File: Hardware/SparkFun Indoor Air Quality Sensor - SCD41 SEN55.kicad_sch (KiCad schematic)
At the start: 38 parts, among them J1 Qwiic_RA, J2 Qwiic_RA, J3 Conn_01x04, U1 AP3012, U1 SEN55, U3 SCD41, U4 SEN55_Outline

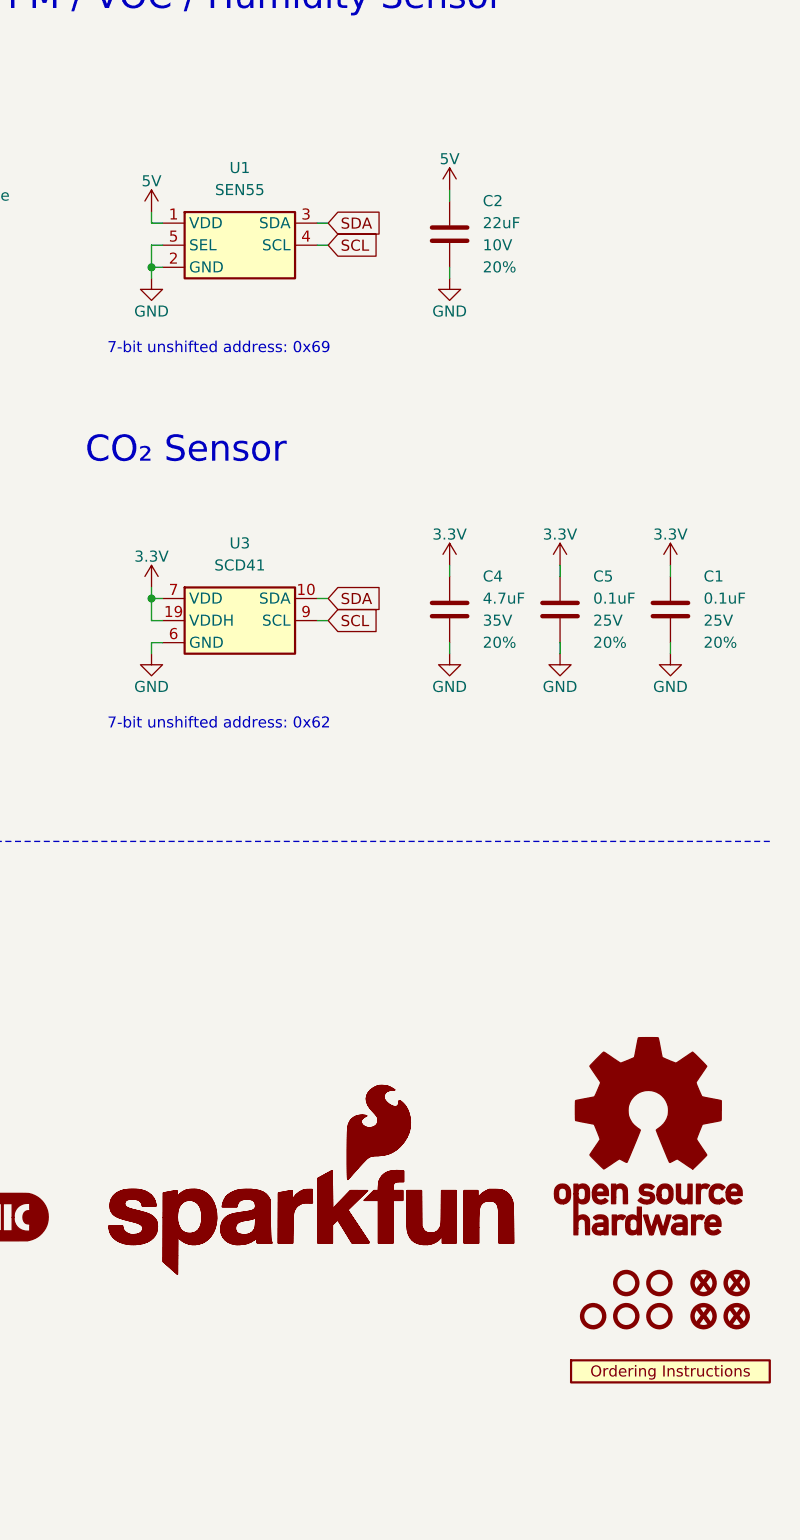
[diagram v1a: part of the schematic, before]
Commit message: Fix PROD_ID on SEN55 connector and module.
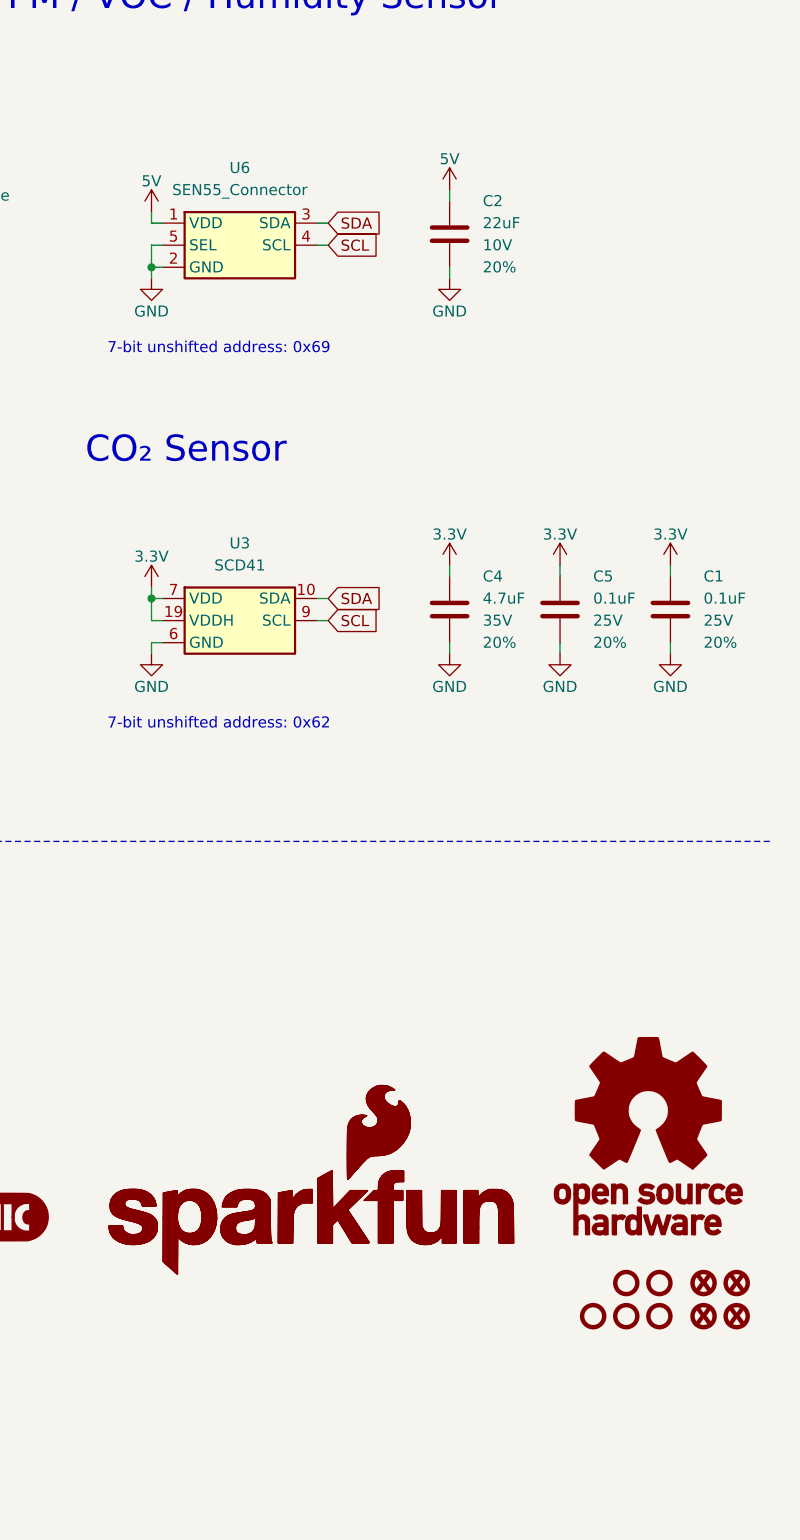
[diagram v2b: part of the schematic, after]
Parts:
- removed U1: SEN55, SparkFun-Connector:JST_SMD_1.25mm-6_Locking, symbol SparkFun-Sensor:SEN55
- removed U2: ~, SparkFun-Aesthetic:Ordering_Instructions, symbol SparkFun-Aesthetic:Ordering_Instructions
- added U6: SEN55_Connector, SparkFun-Connector:JST_SMD_1.25mm-6_Locking, symbol SparkFun-Sensor:SEN55_Connector
- U4: PROD_ID (none) -> COMP-20319
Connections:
- net 5V: now also U6.1 (VDD)
- net GND: now also U6.2 (GND), U6.5 (SEL)
- net SCL: now also U6.4 (SCL)
- net SDA: now also U6.3 (SDA)
- new net: U6.6 (NC), U6.NC1 (NC), U6.NC2 (NC)

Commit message: Update 3D models
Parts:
- D1: footprint SparkFun-LED:LED_0603_1608Metric -> SparkFun-LED:LED_0603_1608Metric_Red
- U3: footprint SparkFun-Sensor:SCD4X -> SparkFun-Sensor:SCD4x
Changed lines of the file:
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@@
 			)
 		)
-		(property "Footprint" "SparkFun-LED:LED_0603_1608Metric"
+		(property "Footprint" "SparkFun-LED:LED_0603_1608Metric_Red"
 			(at 60.96 128.27 0)
 			(effects
@@
 			)
 		)
-		(property "Footprint" "SparkFun-Sensor:SCD4X"
+		(property "Footprint" "SparkFun-Sensor:SCD4x"
 			(at 203.835 107.95 0)
 			(effects
